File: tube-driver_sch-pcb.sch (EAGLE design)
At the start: 108 parts, among them CN1 KS 54, CN10 NO FIT, CN2 MUSB-05-S-B-SM-A, CN3 KS 54, CN4 KS 54, CN5 KS 54, CN6 KS 54, CN7 KS 54, CN8 KS 54, CN9 KS 54, Q4 MMBT3904, Q5 MMBT3904, SW1 RA SM TACT, SW2 RA SM TACT, SW3 RA SM TACT, U1 STM32L052C8, U10 TPS61500, U2 TPS61500, U3 TPS61500, U5 ESP32, U6 USBLC6-2SC6, U7 FT231X, U8 TPS61500

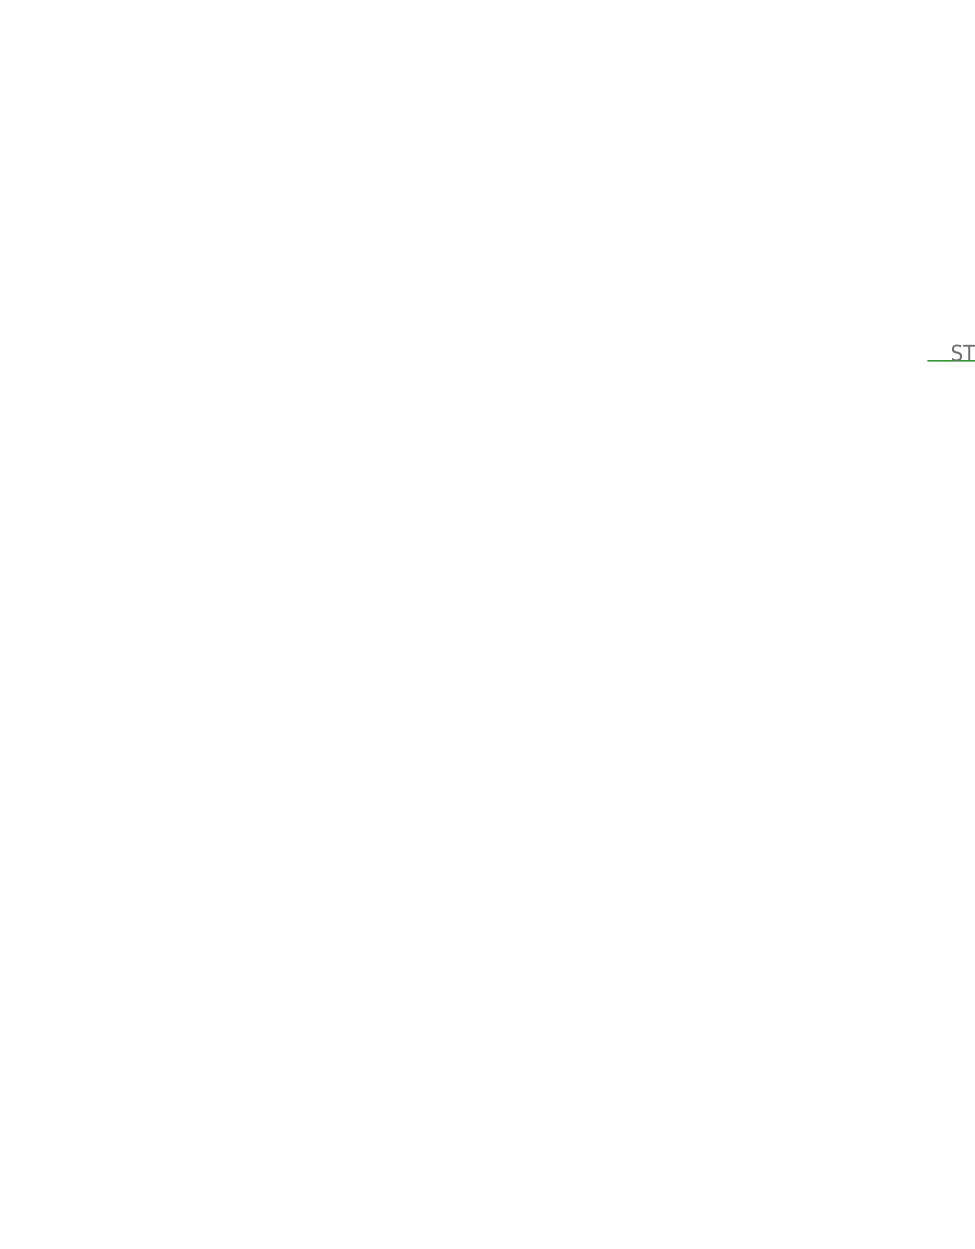
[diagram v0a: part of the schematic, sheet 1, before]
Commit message: First revision done, need to test ESP32 SPi
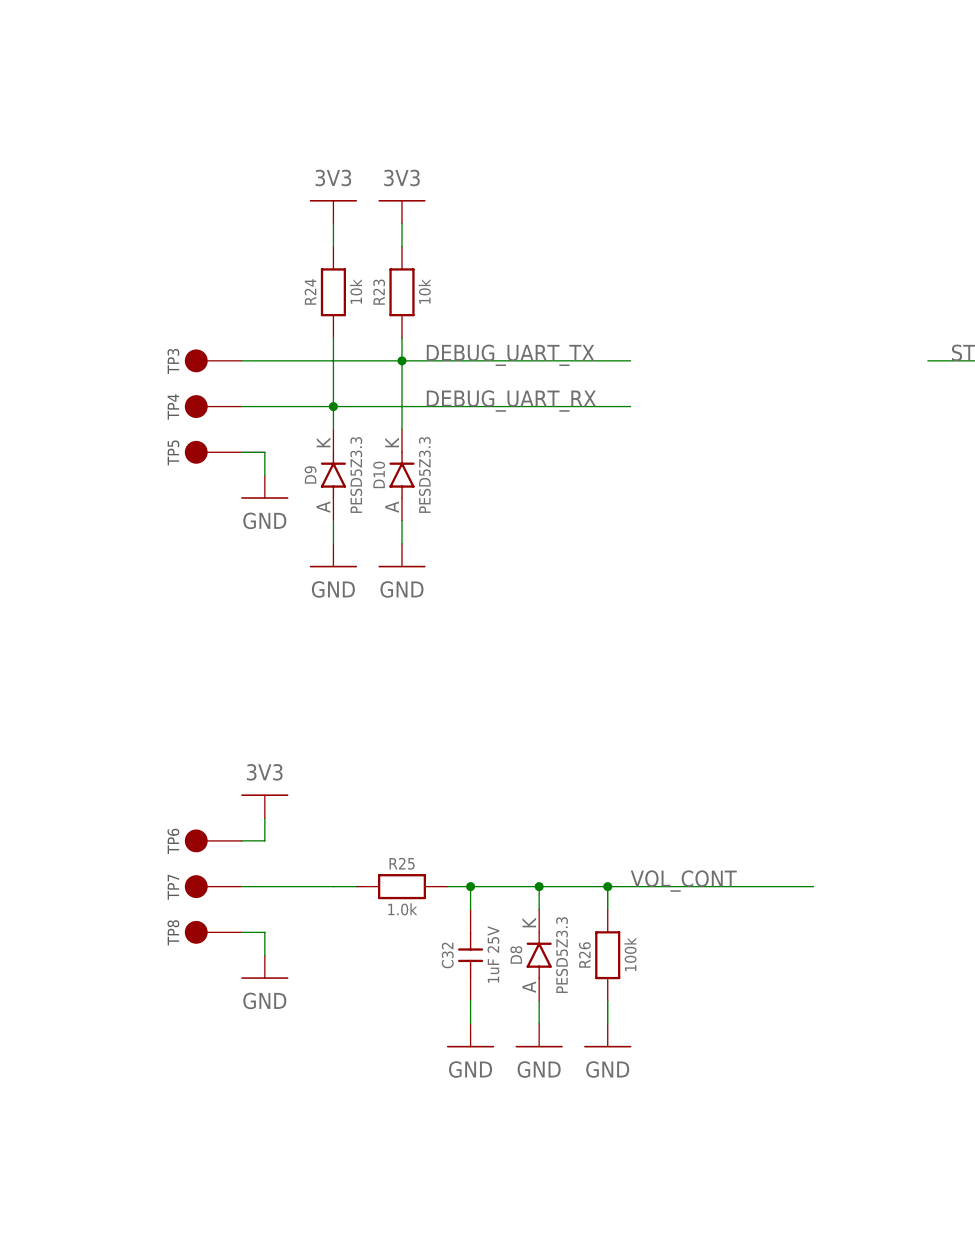
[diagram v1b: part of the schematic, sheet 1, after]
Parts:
- added C29, C30: 22uF 10V, CAPACITORS:CL31B226MPHNNNE
- added C31, C7: 10uF 50V, CAPACITORS:C3225X7S1H106M250AB
- added C32: 1uF 25V, CAPACITORS:CL10A105KA8NNNC
- added D1, D4: B360A-13-F, DIODES:B360A-13-F
- added D10, D8, D9: PESD5Z3.3, DIODES:PESD5Z3.3
- added D6: B0540W, DIODES:B0540W
- added R23, R24: 10k, r_0603:ERJ3EKF1002V
- added R25: 1.0k, r_0603:ERJ3EKF1001V
- added R26: 100k, r_0603:ERJ3EKF1003V
- added TP1, TP2, TP3, TP4, TP5, TP6, TP7, TP8: 2MM_TEST_POINT, MISC:2MM_TEST_POINT
- added U11: 3.3V BUCK, ICs:LMZM23600V3SILT
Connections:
- new net N$4: R25.1, TP7.P$1
- new net N$5: D1.A, D4.A, TP1.P$1
- net 3V3: now also C29.2, C30.2, R23.2, R24.2, TP6.P$1, U11.FB, U11.VOUT
- net DEBUG_UART_RX: now also D9.K, R24.1, TP4.P$1
- net DEBUG_UART_TX: now also D10.K, R23.1, TP3.P$1
- net GND: now also C29.1, C30.1, C31.1, C32.1, C7.1, D10.A, D6.A, D8.A, D9.A, R26.1, TP2.P$1, TP5.P$1, TP8.P$1, U11.GND, U11.MODE/SYNC
- net VIN: now also C31.2, C7.2, D1.K, D4.K, D6.K, U11.EN, U11.VIN
- net VOL_CONT: now also C32.2, D8.K, R25.2, R26.2

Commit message: Driver passes DRC ready to create outputs
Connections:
- removed net LED_PWM: U5.IO17
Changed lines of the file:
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@@
 <?xml version="1.0" encoding="utf-8"?>
 <!DOCTYPE eagle SYSTEM "eagle.dtd">
-<eagle version="9.3.2">
+<eagle version="9.3.0">
 <drawing>
 <settings>
@@
 </segment>
 </net>
-<net name="LED_PWM" class="0">
-<segment>
-<pinref part="U5" gate="G$1" pin="IO17"/>
-<wire x1="375.92" y1="91.44" x2="408.94" y2="91.44" width="0.1524" layer="91"/>
-<wire x1="408.94" y1="91.44" x2="411.48" y2="91.44" width="0.1524" layer="91"/>
-<label x="378.46" y="91.44" size="1.778" layer="95"/>
-</segment>
-</net>

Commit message: Changing ESP32 and STM32 interface to UART
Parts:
- removed D10, D9: PESD5Z3.3, DIODES:PESD5Z3.3
- removed R23, R24: 10k, r_0603:ERJ3EKF1002V
- removed TP3, TP4, TP5: 2MM_TEST_POINT, MISC:2MM_TEST_POINT
- added C33: 100nF 16V, CAPACITORS:CL10B104KO8WPNC
- added R32: 10k, r_0603:ERJ3EKF1002V
- added R33: 120R, r_0603:ERJ3EKF1200V
- added TP10, TP11, TP9: 2MM_TEST_POINT, MISC:2MM_TEST_POINT
- added U12: SN65HVD75D, ICs:SN65HVD75D
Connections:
- removed net DEBUG_UART_RX: D9.K, R24.1, TP4.P$1, U1.PA10
- removed net DEBUG_UART_TX: D10.K, R23.1, TP3.P$1, U1.PA9
- removed net ESP_SPI_CS: U1.PA4, U5.IO15
- removed net ESP_SPI_MISO: U1.PA6, U5.IO26
- removed net ESP_SPI_MOSI: U1.PA7, U5.IO27
- removed net ESP_SPI_SCLK: U1.PA5, U5.IO25
- removed net ESP_SPI_SS: U5.IO32
- new net ESP_UART_RX: U1.PA2
- new net ESP_UART_TX: U1.PA3
- new net RS485_DE: R32.2, U1.PA12, U12.!RE, U12.DE
- new net RS485_UART_RX: U1.PA10, U12.R
- new net RS485_UART_TX: U1.PA9, U12.D
- new net RS485_USR_A: R33.2, TP9.P$1, U12.A
- new net RS485_USR_B: R33.1, TP10.P$1, U12.B
- net 3V3: now also C33.2, U12.VCC; no longer R23.2, R24.2
- net ESP_INT: now also U1.PA4; no longer U1.PA8
- net GND: now also C33.1, R32.1, TP11.P$1, U12.GND; no longer D10.A, D9.A, TP5.P$1
- net LED_PWM_0: now also U1.PA5; no longer U1.PA15
- net LED_PWM_2: now also U1.PB10; no longer U1.PA2
- net LED_PWM_3: now also U1.PB11; no longer U1.PA3
- net USER_BTN_1: now also U1.PB0; no longer U1.PA12

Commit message: ESP and STM UART link established
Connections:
- net ESP_UART_RX: now also U5.IO16
- net ESP_UART_TX: now also U5.IO17
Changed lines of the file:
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@@
 <?xml version="1.0" encoding="utf-8"?>
 <!DOCTYPE eagle SYSTEM "eagle.dtd">
-<eagle version="9.5.1">
+<eagle version="9.3.2">
 <drawing>
 <settings>
@@
 <label x="220.98" y="276.86" size="1.778" layer="95"/>
 </segment>
+<segment>
+<pinref part="U5" gate="G$1" pin="IO16"/>
+<wire x1="375.92" y1="93.98" x2="411.48" y2="93.98" width="0.1524" layer="91"/>
+<label x="378.46" y="93.98" size="1.778" layer="95"/>
+</segment>
 </net>
 <net name="ESP_UART_TX" class="0">
@@
 <label x="220.98" y="274.32" size="1.778" layer="95"/>
 </segment>
-</net>
+<segment>
+<pinref part="U5" gate="G$1" pin="IO17"/>
+<wire x1="375.92" y1="91.44" x2="411.48" y2="91.44" width="0.1524" layer="91"/>
+<label x="378.46" y="91.44" size="1.778" layer="95"/>
+</segment>
+</net>

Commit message: First revision of the driver complete
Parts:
- added R23, R24: 0R, RESISTORS:CRCW06030000Z0EA
- added R34: 5.1k, r_0603:ERJ3EKF5101V
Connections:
- new net ESP_IO13: R23.2, U5.IO13
- new net ESP_IO15: R24.2, U5.IO15
- new net N$13: R34.1, U5.IO2
- net ESP32_UART_!DTR: now also R24.1
- net ESP32_UART_!RTS: now also R23.1
- net GND: now also R34.2
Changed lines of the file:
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@@
 <?xml version="1.0" encoding="utf-8"?>
 <!DOCTYPE eagle SYSTEM "eagle.dtd">
-<eagle version="9.3.2">
+<eagle version="9.5.1">
 <drawing>
 <settings>
@@
 <part name="TP11" library="MISC" deviceset="2MM_TEST_POINT" device=""/>
 <part name="GND79" library="NETS" deviceset="GND" device=""/>
+<part name="R23" library="RESISTORS" deviceset="CRCW06030000Z0EA" device="" value="0R"/>
+<part name="R24" library="RESISTORS" deviceset="CRCW06030000Z0EA" device="" value="0R"/>
+<part name="R34" library="r_0603" deviceset="ERJ3EKF5101V" device="" value="5.1k"/>
 </parts>
 <sheets>
@@
 <attribute name="VALUE" x="-2.54" y="312.42" size="1.778" layer="96" align="center"/>
 </instance>
+<instance part="R23" gate="G$1" x="233.68" y="134.62" smashed="yes">
+<attribute name="NAME" x="233.68" y="137.16" size="1.27" layer="95" align="center"/>
+<attribute name="VALUE" x="233.68" y="132.08" size="1.27" layer="96" align="center"/>
+</instance>
+<instance part="R24" gate="G$1" x="233.68" y="127" smashed="yes">
+<attribute name="NAME" x="233.68" y="129.54" size="1.27" layer="95" align="center"/>
+<attribute name="VALUE" x="233.68" y="124.46" size="1.27" layer="96" align="center"/>
+</instance>
+<instance part="R34" gate="G$1" x="383.54" y="119.38" smashed="yes">
+<attribute name="NAME" x="383.54" y="121.92" size="1.27" layer="95" align="center"/>
+<attribute name="VALUE" x="383.54" y="116.84" size="1.27" layer="96" align="center"/>
+</instance>
 </instances>
 <busses>
@@
 <pinref part="GND79" gate="G$1" pin="GND"/>
 <wire x1="-2.54" y1="320.04" x2="-2.54" y2="317.5" width="0.1524" layer="91"/>
+</segment>
+<segment>
+<wire x1="388.62" y1="119.38" x2="411.48" y2="119.38" width="0.1524" layer="91"/>
+<pinref part="R34" gate="G$1" pin="2"/>
+<label x="391.16" y="119.38" size="1.778" layer="95"/>
 </segment>
 </net>
@@
 <label x="251.46" y="71.12" size="1.778" layer="95"/>
 </segment>
+<segment>
+<pinref part="R23" gate="G$1" pin="1"/>
+<wire x1="228.6" y1="134.62" x2="198.12" y2="134.62" width="0.1524" layer="91"/>
+<label x="200.66" y="134.62" size="1.778" layer="95"/>
+</segment>
 </net>
 <net name="ESP32_UART_!DTR" class="0">
@@
 <junction x="248.92" y="93.98"/>
 <label x="251.46" y="93.98" size="1.778" layer="95"/>
+</segment>
+<segment>
+<pinref part="R24" gate="G$1" pin="1"/>
+<wire x1="228.6" y1="127" x2="198.12" y2="127" width="0.1524" layer="91"/>
+<label x="200.66" y="127" size="1.778" layer="95"/>
 </segment>
 </net>
@@
 </segment>
 </net>
+<net name="ESP_IO13" class="0">
+<segment>
+<pinref part="U5" gate="G$1" pin="IO13"/>
+<wire x1="375.92" y1="101.6" x2="411.48" y2="101.6" width="0.1524" layer="91"/>
+<label x="378.46" y="101.6" size="1.778" layer="95"/>
+</segment>
+<segment>
+<pinref part="R23" gate="G$1" pin="2"/>
+<wire x1="238.76" y1="134.62" x2="269.24" y2="134.62" width="0.1524" layer="91"/>
+<label x="241.3" y="134.62" size="1.778" layer="95"/>
+</segment>
+</net>
+<net name="ESP_IO15" class="0">
+<segment>
+<pinref part="U5" gate="G$1" pin="IO15"/>
+<wire x1="375.92" y1="96.52" x2="411.48" y2="96.52" width="0.1524" layer="91"/>
+<label x="378.46" y="96.52" size="1.778" layer="95"/>
+</segment>
+<segment>
+<pinref part="R24" gate="G$1" pin="2"/>
+<wire x1="238.76" y1="127" x2="269.24" y2="127" width="0.1524" layer="91"/>
+<label x="241.3" y="127" size="1.778" layer="95"/>
+</segment>
+</net>
+<net name="N$13" class="0">
+<segment>
+<pinref part="U5" gate="G$1" pin="IO2"/>
+<wire x1="375.92" y1="119.38" x2="378.46" y2="119.38" width="0.1524" layer="91"/>
+<pinref part="R34" gate="G$1" pin="1"/>
+</segment>
+</net>

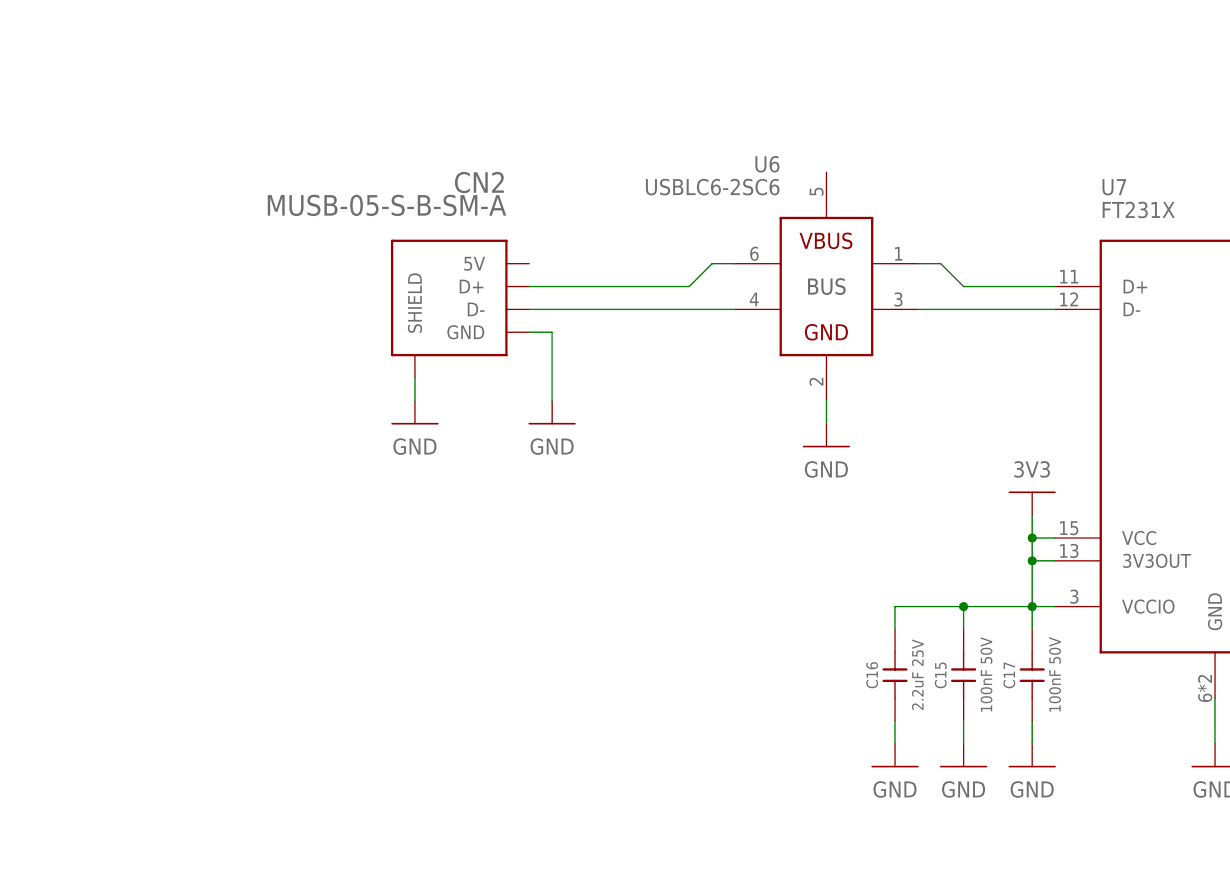
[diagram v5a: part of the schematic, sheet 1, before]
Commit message: Improved BoM
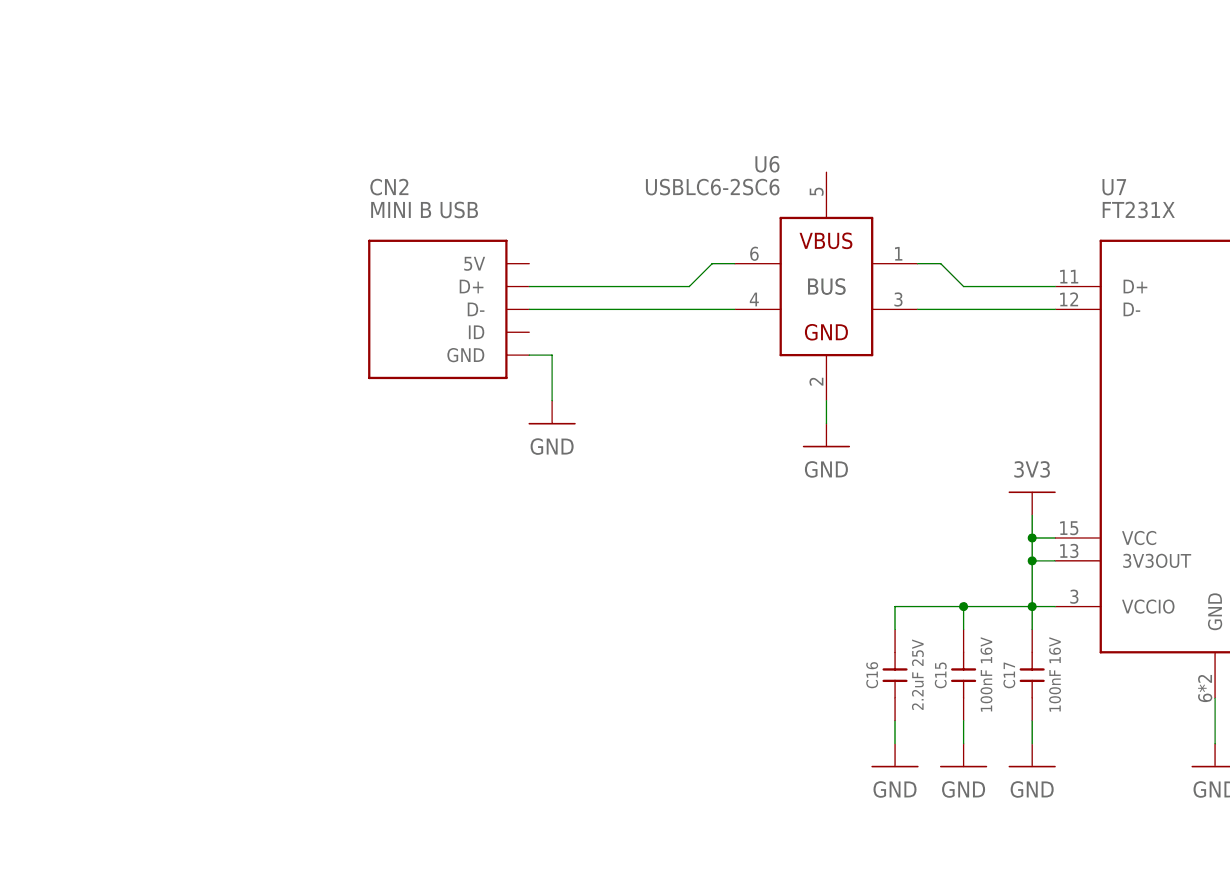
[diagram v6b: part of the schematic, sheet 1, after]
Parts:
- C15: value 100nF 50V -> 100nF 16V; device CAPACITORS:VJ0603Y104KXACW1BC -> CAPACITORS:CL10B104KO8WPNC; FARNELL 2407338 -> (none); PRICE_PER 0.0085 -> (none); VALUE 100nF 50V -> (none)
- C17: value 100nF 50V -> 100nF 16V; device CAPACITORS:VJ0603Y104KXACW1BC -> CAPACITORS:CL10B104KO8WPNC; VALUE 100nF 50V -> (none)
- CN2: value MUSB-05-S-B-SM-A -> MINI B USB
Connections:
- net GND: no longer CN2.SHIELD
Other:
- moved on the sheet: CN2

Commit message: Working on rev 2
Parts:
- removed C15, C17, C33, C5, C6: 100nF 16V, CAPACITORS:CL10B104KO8WPNC
- removed C16: 2.2uF 25V, CAPACITORS:GRM188R61E225KA12D
- removed CN10: NO FIT, CONNECTORs:TSM-103-03-T-DV
- removed R18: 1.0k, r_0603:ERJ3EKF1001V
- removed R32, R5: 10k, r_0603:ERJ3EKF1002V
- removed R33: 120R, r_0603:ERJ3EKF1200V
- removed SW2, SW3: RA SM TACT, ELECTROMECH:EVQ-P7J01P
- removed TP10, TP11, TP9: 2MM_TEST_POINT, MISC:2MM_TEST_POINT
- removed U12: SN65HVD75D, ICs:SN65HVD75D
- removed U7: FT231X, ICs:FT231X
- added D9: B360A-13-F, DIODES:B360A-13-F
- added FB1: 150R 100MHz, INDUCTORS:ILB1206ER151V
- C2: value 100nF 16V -> 4.7uF 6.3V; device CAPACITORS:CL10B104KO8WPNC -> CAPACITORS:GRM188R60J475ME19D
- C4: value 100nF 16V -> 1nF 50V; device CAPACITORS:CL10B104KO8WPNC -> CAPACITORS:CL10B102KB8NNNC
- R2: value 10k -> 20k; device r_0603:ERJ3EKF1002V -> r_0603:ERJ3EKF2002V
- R4: value 1.0k -> 2.2k; device r_0603:ERJ3EKF1001V -> r_0603:ERJ3EKF2201V
- U1: value STM32L052C8 -> CP2102; device ICs:STM32L052C8T6 -> ICs:CP2102N-A01-GQFN28
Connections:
- removed net ESP_INT: U1.PA4, U5.IO33
- removed net ESP_UART_RX: U1.PA2, U5.IO16
- removed net ESP_UART_TX: U1.PA3, U5.IO17
- removed net RS485_DE: R32.2, U1.PA12, U12.!RE, U12.DE
- removed net RS485_UART_RX: U1.PA10, U12.R
- removed net RS485_UART_TX: U1.PA9, U12.D
- removed net RS485_USR_A: R33.2, TP9.P$1, U12.A
- removed net RS485_USR_B: R33.1, TP10.P$1, U12.B
- removed net STM_NRST: CN10.3, R2.1, U1.NRST
- removed net STM_SWCLK: CN10.4, U1.PA14
- removed net STM_SWDIO: CN10.5, U1.PA13
- removed net USER_BTN_0: C5.2, R4.1, U1.PA11
- removed net USER_BTN_1: C6.2, R18.1, U1.PB0
- new net 5VUSB: C3.2, C4.2, D9.A, FB1.2, R1.1, U6.VBUS
- new net N$20: CN2.5V, FB1.1
- new net N$7: C1.2, C2.2, U1.VDD, U1.VREGIN
- net 3V3: now also R4.2; no longer C1.2, C15.2, C16.2, C17.2, C2.2, C3.2, C33.2, C4.2, CN10.1, R2.2, R3.2, R5.2, U1.VDD, U1.VDDA, U12.VCC, U7.!RESET, U7.3V3OUT, U7.VCC, U7.VCCIO
- net ESP32_UART_!DTR: now also U1.DTR; no longer U7.!DTR
- net ESP32_UART_!RTS: now also U1.RTS; no longer U7.!RTS
- net ESP32_UART_RX: now also U1.TXD; no longer U7.TXD
- net ESP32_UART_TX: now also U1.RXD; no longer U7.RXD
- net GND: now also R2.1, R3.1, U1.GND; no longer C15.1, C16.1, C17.1, C33.1, C5.1, C6.1, CN10.6, R1.1, R32.1, SW2.2, SW3.2, TP11.P$1, U1.VSS, U1.VSSA, U12.GND, U7.GND
- net LED_PWM_0: no longer U1.PA5
- net LED_PWM_1: no longer U1.PA1
- net LED_PWM_2: no longer U1.PB10
- net LED_PWM_3: no longer U1.PB11
- net N$1: now also R2.2, U1.VBUS; no longer U1.BOOT0
- net N$2: now also R4.1, U1.!RST; no longer R3.1, R4.2, SW2.1
- net N$3: now also R3.2, U1.!SUSPEND; no longer R18.2, R5.1, SW3.1
- net N$97: now also U1.D-; no longer U7.D-
- net N$98: now also U1.D+; no longer U7.D+
- net VIN: now also D9.K
- net VOL_CONT: no longer U1.PA0
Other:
- moved on the sheet: C1, C2, C20, C3, C32, C4, CN2, D8, R1, R11, R16, R2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
